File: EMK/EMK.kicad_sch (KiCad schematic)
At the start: 18 parts, among them U1 nRF52840-QFAA, U2 15nH, Y1 Crystal_32.768kHz, Y2 Crystal_32mHz

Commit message: feat: adiciona o power management
Signed-off-by: Paulo Santos <prms@ic.ufal.br>
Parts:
- added C14, C15, C18: 4.7uF, symbol Device:C
- added C16: 120pF, symbol Device:C
- added C17: 22uF, symbol Device:C
- added D1: D_Schottky, symbol Device:D_Schottky
- added D2, D3: LED, symbol Device:LED
- added J1: USB_C_Receptacle_USB2.0_14P, symbol EMKPower:USB_C_Receptacle_USB2.0_14P
- added J2: Conn_01x02_Socket, symbol Connector:Conn_01x02_Socket
- added L2: 470nH 15mOhm, symbol Device:L
- added Q1: Si2371EDS, Package_TO_SOT_SMD:SOT-23, symbol EMKPower:Si2371EDS
- added R1, R2: 5.1k, symbol Device:R
- added R3, R5: 100k, symbol Device:R
- added R4: 453k, symbol Device:R
- added R6, R7: 1k, symbol Device:R
- added R8: 2M, symbol Device:R
- added R9: 806k, symbol Device:R
- added SW1: SW_Nidec_CAS-120A1, Button_Switch_SMD:Nidec_Copal_CAS-120A, symbol Switch:SW_Nidec_CAS-120A1
- added U3: TPS62822DLC, Package_SON:Texas_VSON-HR-8_1.5x2mm_P0.5mm, symbol EMKPower:TPS62822DLC
- added U4: USBLC6-2SC6, Package_TO_SOT_SMD:SOT-23-6, symbol EMKPower:USBLC6-2SC6
- added U5: TP4057, Package_TO_SOT_SMD:TSOT-23-5, symbol EMKPower:TP4057
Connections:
- net VDD_NRF: now reaches C11.1, U1.12 (VDD)
- net VDD_NRF: now also C16.1, C17.1, L2.2, R4.1
- net at U1.4 (P0.04/AIN2): now also R8.1, R9.2
- new net: D2.2 (A), D3.2 (A), R6.2
- new net: C14.1, C15.1, D1.1 (K), Q1.2 (S), U3.1 (EN), U3.7 (VIN)
- new net: Q1.3 (D), SW1.2 (B)
- new net: J1.A5 (CC1), R1.1
- new net: J1.B5 (CC2), R2.1
- new net: C16.2, R4.2, R5.1, U3.2 (FB)
- new net: L2.1, U3.6 (SW)
- new net: D2.1 (K), U5.1 (~{CHRG})
- new net: R7.1, U5.6 (PROG)
- new net: D3.1 (K), U5.5 (STDBY)
- new net GND: C14.2, C15.2, C17.2, C18.2, J1.A1 (GND), J1.A12 (GND), J1.B1 (GND), J1.B12 (GND), J1.S1 (SHIELD), J2.1 (Pin_1), R1.2, R2.2, R3.2, R5.2, R7.2, R8.2, U3.3 (AGND), U3.5 (PGND), U5.2 (GND)
- new net J_D+: J1.A6 (D+), J1.B6 (D+), U4.1 (I/O1)
- new net J_D-: J1.A7 (D-), J1.B7 (D-), U4.6 (I/O1)
- new net M_D+: U4.3 (I/O2)
- new net M_D-: U4.4 (I/O2)
- new net VBAT: C18.1, J2.2 (Pin_2), R9.1, SW1.1 (C), U5.3 (BAT)
- new net VBUS: D1.2 (A), J1.A4 (VBUS), J1.A9 (VBUS), J1.B4 (VBUS), J1.B9 (VBUS), Q1.1 (G), R3.1, R6.1, U4.5 (VBUS), U5.4 (V_{CC})

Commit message: wip: Introduz a matriz de botões ao esquemático.
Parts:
- added D10, D11, D4, D5, D6, D7, D8, D9: D, symbol Device:D
- added J3: Conn_ARM_JTAG_SWD_10, symbol Connector:Conn_ARM_JTAG_SWD_10
- added SW2, SW3, SW4, SW5, SW6, SW7, SW8, SW9: SW_Push, symbol Switch:SW_Push
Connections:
- new net: D7.2 (A), SW5.1
- new net: D10.2 (A), SW8.1
- new net: D6.2 (A), SW4.1
- new net: D9.2 (A), SW7.1
- new net: J3.3 (GND), J3.5 (GND)
- new net: D8.2 (A), SW6.1
- new net: D5.2 (A), SW3.1
- new net: D11.2 (A), SW9.1
- new net: D4.2 (A), SW2.1
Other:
- added sheet Matriz (untitled.kicad_sch)
- moved on the sheet: C1, C10, C11, C12, C13, C14, C15, C16, C17, C18, C2, C3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

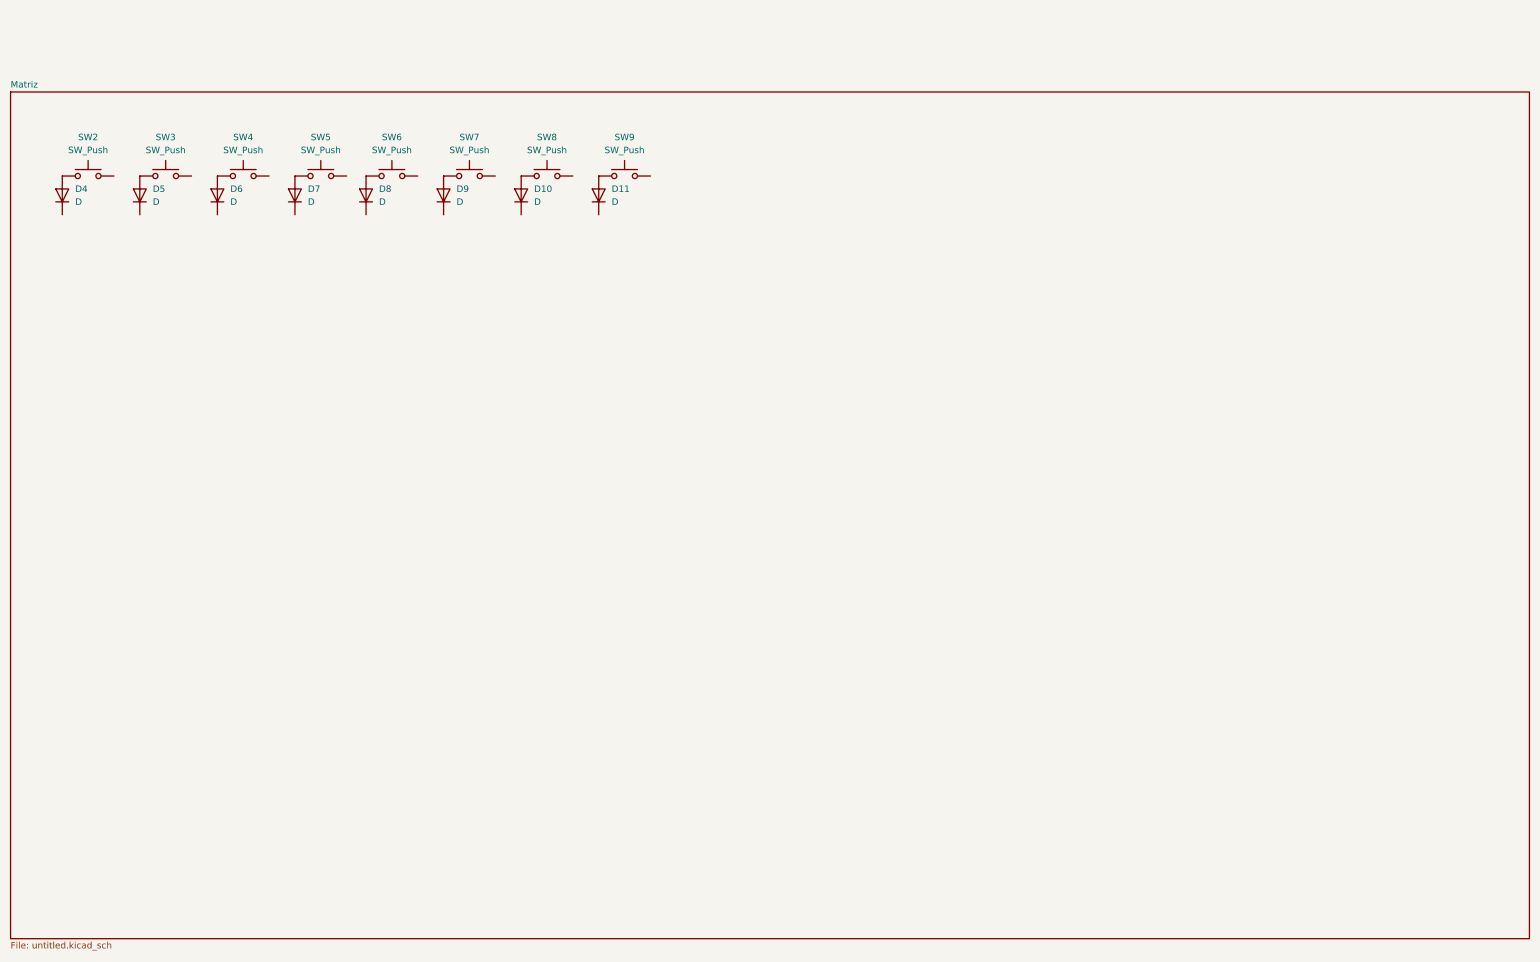
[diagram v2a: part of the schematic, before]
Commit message: feat: adiciona a matriz de switches.
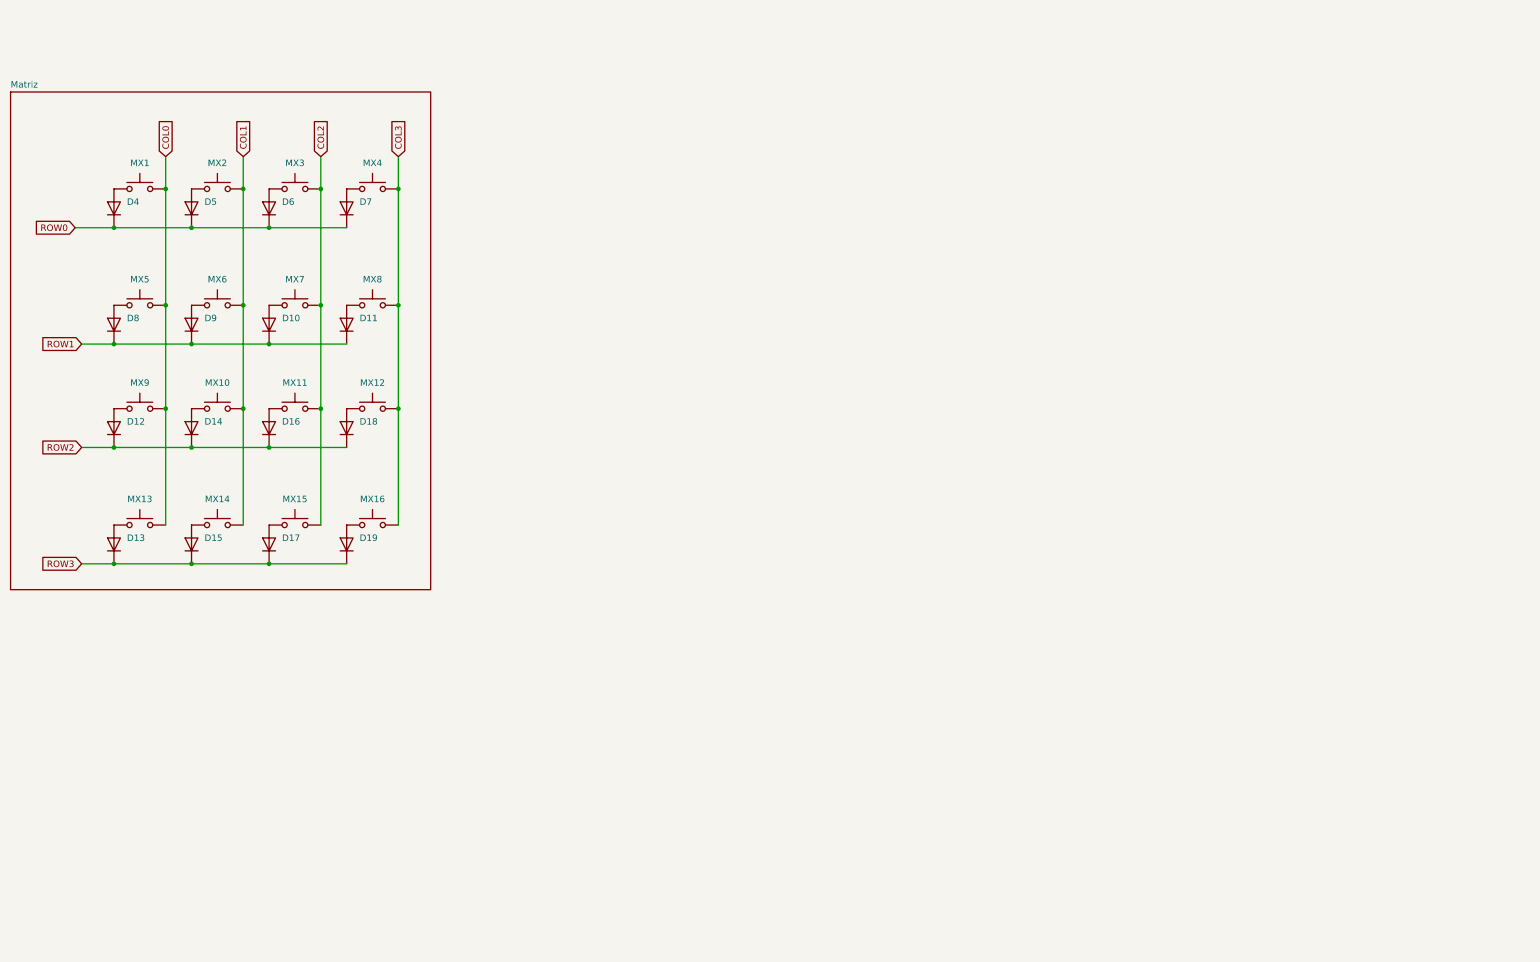
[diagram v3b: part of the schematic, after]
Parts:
- added D12, D13, D14, D15, D16, D17, D18, D19: D, symbol Device:D
- added SW10: MX9, symbol Switch:SW_Push
- added SW11: MX13, symbol Switch:SW_Push
- added SW12: MX10, symbol Switch:SW_Push
- added SW13: MX14, symbol Switch:SW_Push
- added SW14: MX11, symbol Switch:SW_Push
- added SW15: MX15, symbol Switch:SW_Push
- added SW16: MX12, symbol Switch:SW_Push
- added SW17: MX16, symbol Switch:SW_Push
- SW2: value SW_Push -> MX1
- SW3: value SW_Push -> MX2
- SW4: value SW_Push -> MX3
- SW5: value SW_Push -> MX4
- SW6: value SW_Push -> MX5
- SW7: value SW_Push -> MX6
- SW8: value SW_Push -> MX7
- SW9: value SW_Push -> MX8
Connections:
- net COL3: now reaches SW5.2
- net COL3: now also SW9.2, SW16.2, SW17.2
- net COL2: now reaches SW8.2
- net COL2: now also SW4.2, SW14.2, SW15.2
- net ROW0: now reaches D6.1 (K)
- net ROW0: now also D4.1 (K), D5.1 (K), D7.1 (K)
- net ROW1: now reaches D9.1 (K)
- net ROW1: now also D10.1 (K), D11.1 (K), D8.1 (K)
- net COL0: now reaches SW6.2
- net COL0: now also SW2.2, SW10.2, SW11.2
- net COL1: now reaches SW3.2
- net COL1: now also SW7.2, SW12.2, SW13.2
- new net: D17.2 (A), SW15.1
- new net: D15.2 (A), SW13.1
- new net: D12.2 (A), SW10.1
- new net: D18.2 (A), SW16.1
- new net: D16.2 (A), SW14.1
- new net: D14.2 (A), SW12.1
- new net: D19.2 (A), SW17.1
- new net: D13.2 (A), SW11.1
- new net ROW2: D12.1 (K), D14.1 (K), D16.1 (K), D18.1 (K)
- new net ROW3: D13.1 (K), D15.1 (K), D17.1 (K), D19.1 (K)
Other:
- moved on the sheet: D10, D11, D4, D5, D6, D7, D8, D9

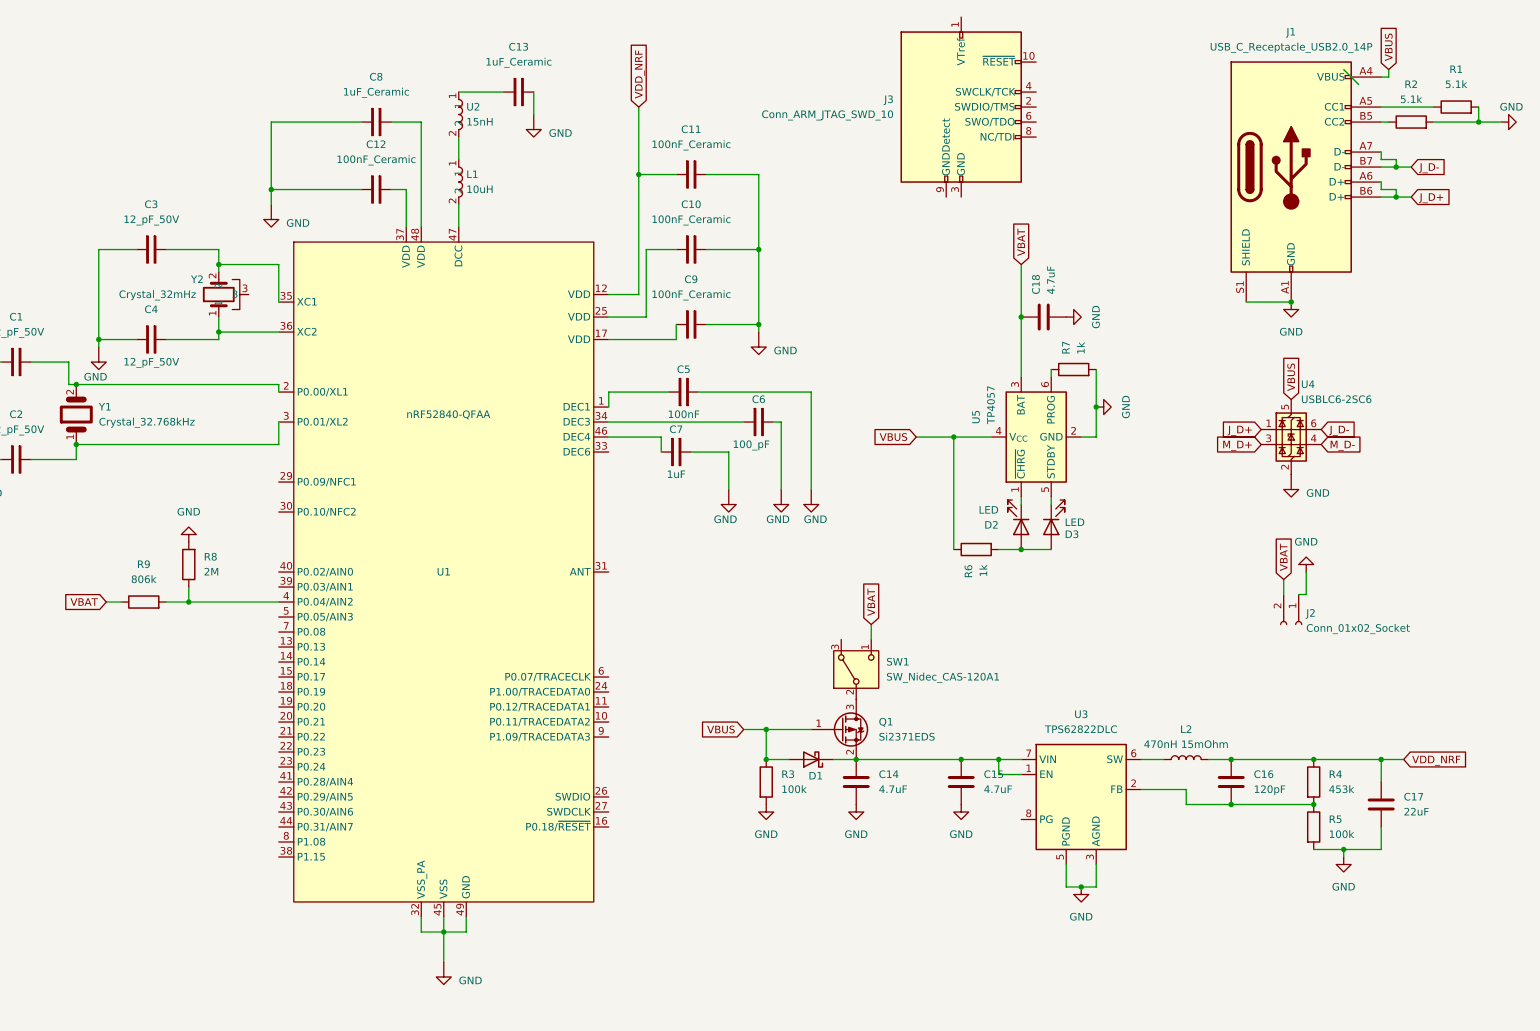
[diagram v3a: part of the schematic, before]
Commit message: feat: adiciona o conector SWD.
Signed-off-by: Paulo Santos <prms@ic.ufal.br>
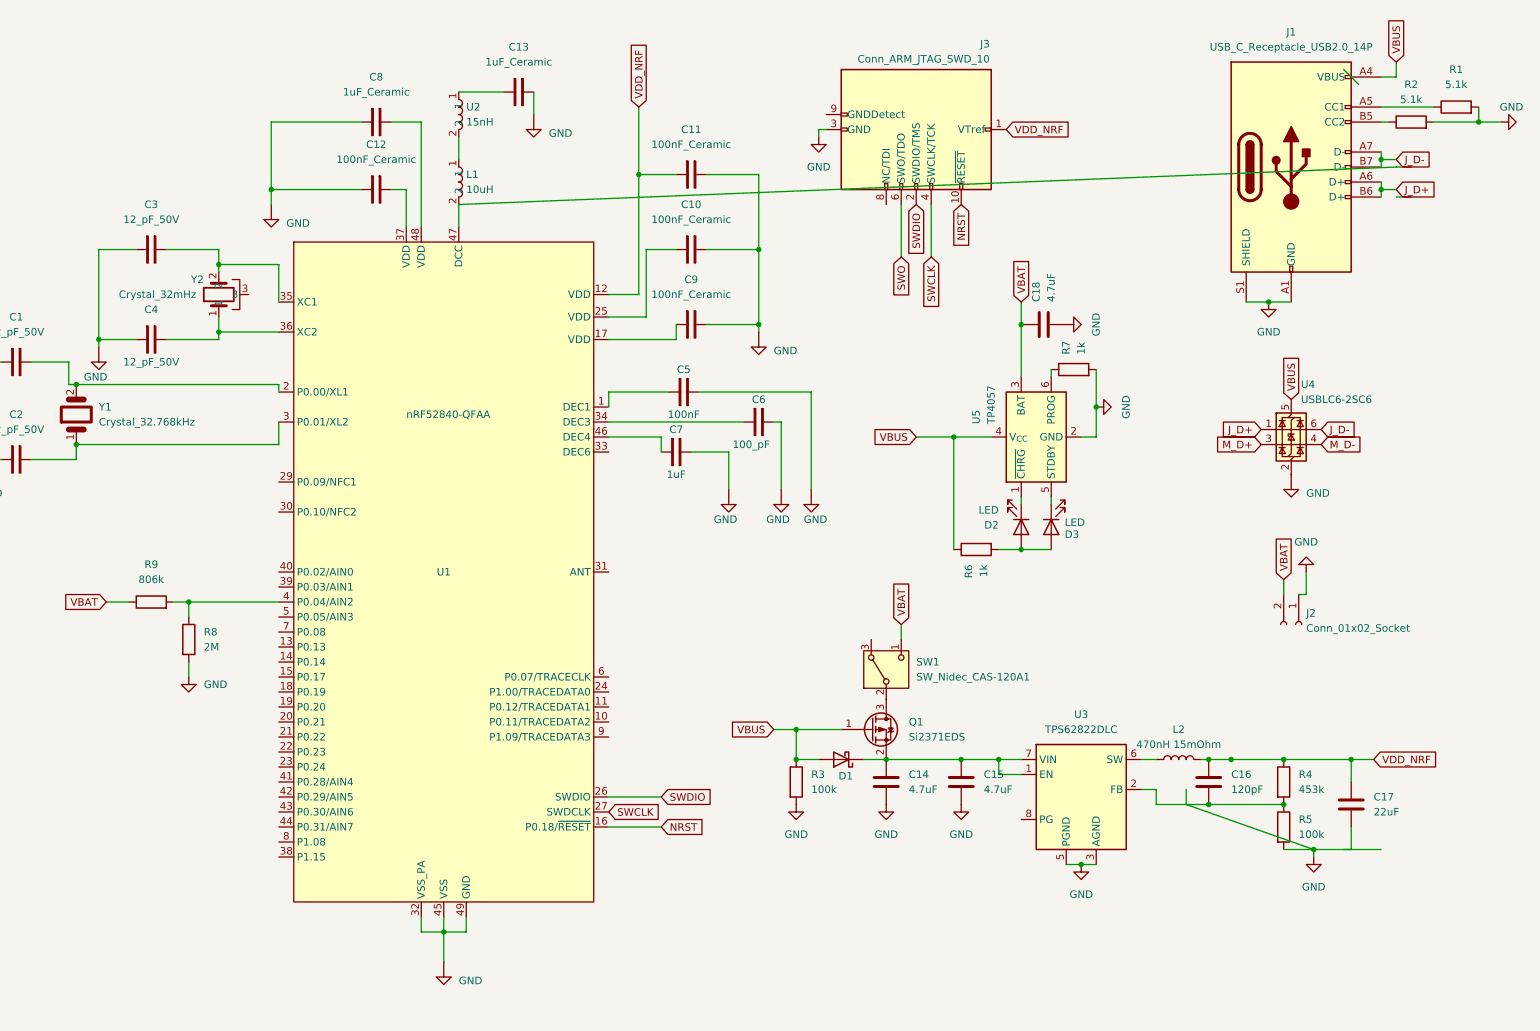
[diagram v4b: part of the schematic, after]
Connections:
- net GND: now also J3.3 (GND), J3.5 (GND)
- net VDD_NRF: now also J3.1 (VTref)
- net NRST: now reaches U1.16 (P0.18/~{RESET})
- net NRST: now also J3.10 (~{RESET})
- net SWDIO: now reaches U1.26 (SWDIO)
- net SWDIO: now also J3.2 (SWDIO/TMS)
- net SWCLK: now reaches U1.27 (SWDCLK)
- net SWCLK: now also J3.4 (SWCLK/TCK)
- net SWO: now reaches J3.6 (SWO/TDO)
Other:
- moved on the sheet: C14, C16, C17, C18, D1, J3, L2, Q1, R3, R4, R5, R8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
